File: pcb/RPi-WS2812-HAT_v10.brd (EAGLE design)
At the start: 65 x 56 mm, 104 parts, among them IC1 24LC-I/OT, IC2 ATTINY85-MU, J1 USB-MICRO, X1 PASSER-07, X2 PASSER-07, X3 PASSER-07

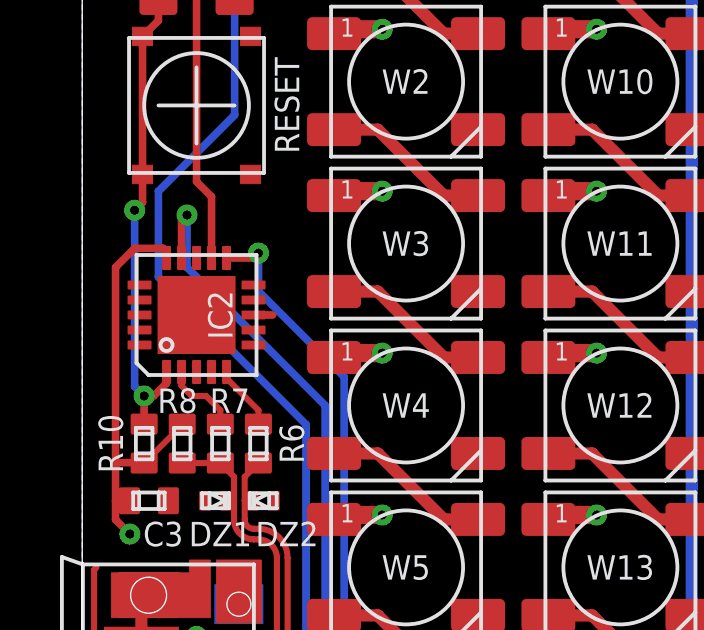
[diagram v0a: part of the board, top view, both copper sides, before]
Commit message: updated layout
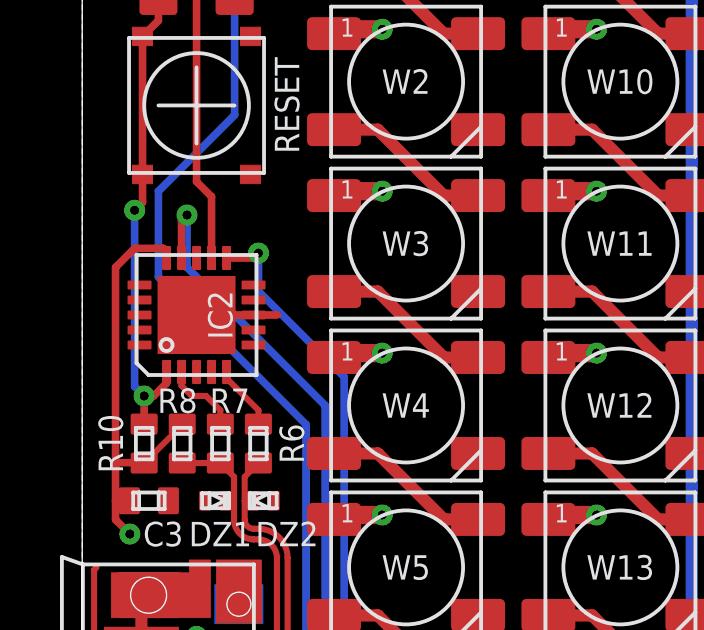
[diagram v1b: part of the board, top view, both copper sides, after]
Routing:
- net GND: track 12.5 -> 13.5 mm
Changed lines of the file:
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@@
 <setting verticaltext="up"/>
 </settings>
-<grid distance="0.05" unitdist="inch" unit="inch" style="lines" multiple="1" display="yes" altdistance="0.025" altunitdist="inch" altunit="inch"/>
+<grid distance="0.05" unitdist="inch" unit="inch" style="lines" multiple="1" display="yes" altdistance="0.00625" altunitdist="inch" altunit="inch"/>
 <layers>
 <layer number="1" name="Top" color="4" fill="1" visible="yes" active="yes"/>
@@
 <text x="0.79375" y="48.41875" size="0.8128" layer="21" font="vector" ratio="10" rot="R90" align="center">MCU</text>
 <text x="32.54375" y="52.3875" size="0.8128" layer="21" font="vector" ratio="10" rot="R180" align="center">Rev 1.0</text>
+<circle x="61.5" y="52.5" radius="1.5" width="0.4064" layer="42"/>
+<circle x="3.5" y="52.5" radius="1.5" width="0.4064" layer="42"/>
+<circle x="61.5" y="3.5" radius="1.5" width="0.4064" layer="42"/>
+<circle x="3.5" y="3.5" radius="1.5" width="0.4064" layer="42"/>
 </plain>
 <attributes>
@@
 <contactref element="R9" pad="1"/>
 <contactref element="C1" pad="1"/>
-<wire x1="5.71" y1="34.44875" x2="6.35" y2="34.44875" width="0.254" layer="1"/>
 <contactref element="GROUND" pad="1"/>
 <wire x1="0.396875" y1="25.955625" x2="0.47625" y2="26.035" width="0.2032" layer="1"/>
@@
 <contactref element="DZ2" pad="A"/>
 <wire x1="5.87375" y1="21.11375" x2="6.50875" y2="21.11375" width="0.3556" layer="1"/>
+<wire x1="5.71" y1="34.44875" x2="4.92125" y2="34.44875" width="0.254" layer="1"/>
+<wire x1="5.71" y1="34.44875" x2="6.50875" y2="34.44875" width="0.254" layer="1"/>
 </signal>
 <signal name="+5V">

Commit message: updated schematics
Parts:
- DZ1, DZ2: value uClamp2511T -> Z3V6
- R8: value 2k2 -> 1k5
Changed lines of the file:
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@@
 </element>
 <element name="DAT" library="we-rcl" package="JUMPER3-0603" value="JUMPER3-0603" x="3.65125" y="48.41875" smashed="yes" rot="R90"/>
-<element name="R8" library="we-rcl" package="R0402" value="2k2" x="3.33375" y="30.1625" smashed="yes">
+<element name="R8" library="we-rcl" package="R0402" value="1k5" x="3.33375" y="30.1625" smashed="yes">
 <attribute name="NAME" x="3.175" y="31.59125" size="0.8128" layer="25" font="vector" ratio="10" align="center"/>
 <attribute name="VALUE" x="3.33375" y="30.1625" size="0.8128" layer="27" font="vector" ratio="10" rot="R270" align="center"/>
@@
 <attribute name="VALUE" x="2.06375" y="30.1625" size="0.8128" layer="27" font="vector" ratio="10" rot="R270" align="center"/>
 </element>
-<element name="DZ1" library="we-rcl" package="SOD882" value="uClamp2511T" x="4.445" y="28.2575" smashed="yes" rot="R270">
+<element name="DZ1" library="we-rcl" package="SOD882" value="Z3V6" x="4.445" y="28.2575" smashed="yes" rot="R270">
 <attribute name="NAME" x="4.60375" y="27.14625" size="0.8128" layer="25" font="vector" ratio="10" rot="R180" align="center"/>
 <attribute name="VALUE" x="4.445" y="26.9875" size="0.8128" layer="27" font="vector" ratio="10" rot="R180" align="center"/>
 </element>
-<element name="DZ2" library="we-rcl" package="SOD882" value="uClamp2511T" x="6.0325" y="28.2575" smashed="yes" rot="R90">
+<element name="DZ2" library="we-rcl" package="SOD882" value="Z3V6" x="6.0325" y="28.2575" smashed="yes" rot="R90">
 <attribute name="NAME" x="6.82625" y="27.14625" size="0.8128" layer="25" font="vector" ratio="10" align="center"/>
 <attribute name="VALUE" x="6.0325" y="29.5275" size="0.8128" layer="27" font="vector" ratio="10" align="center"/>
